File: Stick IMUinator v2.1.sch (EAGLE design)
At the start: 58 parts, among them J001 USB_MICROB_JST, J301 JST 2mm, J401 M06, J701 MICROSD-SOCKET, Q050 PMOS, Q201 PMOS, U101 BMP085, U201 5319, U301 73831, U401 LPC2148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

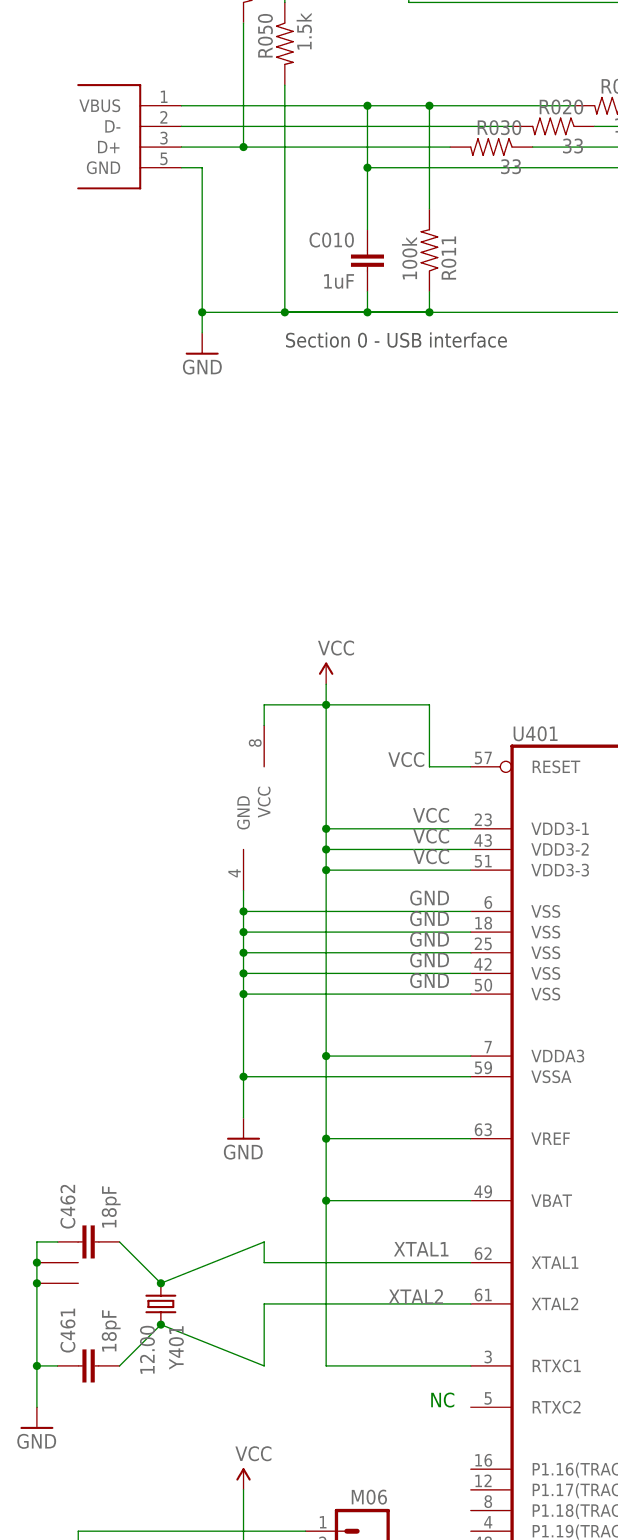
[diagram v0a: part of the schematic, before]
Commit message: Merged Mio's KwanSystems.lbr, updated all eagle files to use it.
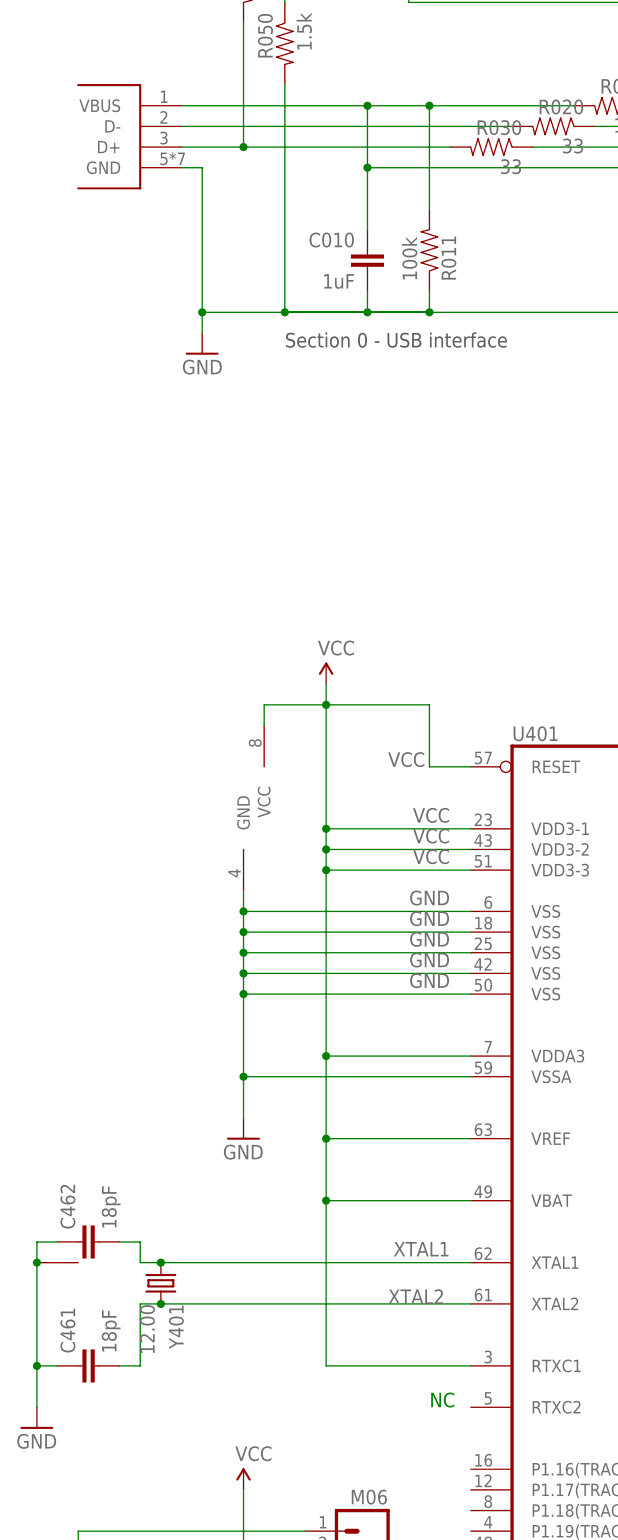
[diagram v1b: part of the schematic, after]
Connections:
- net GND: no longer Y401G$2.1
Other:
- moved on the sheet: Y401
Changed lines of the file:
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@@
 <?xml version="1.0" encoding="utf-8"?>
 <!DOCTYPE eagle SYSTEM "eagle.dtd">
-<eagle version="6.1">
+<eagle version="6.2">
 <drawing>
 <settings>
@@
 <attribute name="DIGIKEY" x="22.86" y="-101.6" size="1.778" layer="96" rot="MR180" display="off"/>
 </instance>
-<instance part="Y401" gate="G$2" x="22.86" y="-104.14" rot="R270"/>
-<instance part="Y401" gate="_" x="38.1" y="-106.68" rot="R270"/>
+<instance part="Y401" gate="_" x="38.1" y="-104.14" rot="R270"/>
 <instance part="R401" gate="A" x="165.1" y="-38.1" rot="R90">
 <attribute name="DIGIKEY" x="165.1" y="-38.1" size="1.778" layer="96" rot="MR180" display="off"/>
@@
 <wire x1="25.4" y1="-99.06" x2="22.86" y2="-99.06" width="0.1524" layer="91"/>
 <wire x1="22.86" y1="-99.06" x2="22.86" y2="-101.6" width="0.1524" layer="91"/>
-<wire x1="22.86" y1="-101.6" x2="22.86" y2="-104.14" width="0.1524" layer="91"/>
-<wire x1="22.86" y1="-104.14" x2="22.86" y2="-114.3" width="0.1524" layer="91"/>
+<wire x1="22.86" y1="-101.6" x2="22.86" y2="-114.3" width="0.1524" layer="91"/>
 <wire x1="22.86" y1="-114.3" x2="22.86" y2="-119.38" width="0.1524" layer="91"/>
 <wire x1="25.4" y1="-114.3" x2="22.86" y2="-114.3" width="0.1524" layer="91"/>
 <junction x="22.86" y="-114.3"/>
 <junction x="22.86" y="-101.6"/>
-<junction x="22.86" y="-104.14"/>
 <pinref part="C462" gate="G$1" pin="1"/>
 <pinref part="C461" gate="G$1" pin="1"/>
 <pinref part="GND2" gate="1" pin="GND"/>
 <pinref part="Y401" gate="G$1" pin="1"/>
-<pinref part="Y401" gate="G$2" pin="1"/>
 </segment>
 <segment>
@@
 <net name="XTAL1" class="0">
 <segment>
-<wire x1="33.02" y1="-99.06" x2="38.1" y2="-104.14" width="0.1524" layer="91"/>
-<wire x1="38.1" y1="-104.14" x2="50.8" y2="-99.06" width="0.1524" layer="91"/>
-<wire x1="50.8" y1="-99.06" x2="50.8" y2="-101.6" width="0.1524" layer="91"/>
-<wire x1="50.8" y1="-101.6" x2="76.2" y2="-101.6" width="0.1524" layer="91"/>
-<junction x="38.1" y="-104.14"/>
+<wire x1="33.02" y1="-99.06" x2="35.56" y2="-99.06" width="0.1524" layer="91"/>
+<wire x1="35.56" y1="-99.06" x2="35.56" y2="-101.6" width="0.1524" layer="91"/>
+<wire x1="35.56" y1="-101.6" x2="38.1" y2="-101.6" width="0.1524" layer="91"/>
+<wire x1="38.1" y1="-101.6" x2="76.2" y2="-101.6" width="0.1524" layer="91"/>
+<junction x="38.1" y="-101.6"/>
 <label x="73.66" y="-99.06" size="1.778" layer="95" rot="R180"/>
 <pinref part="C462" gate="G$1" pin="2"/>
@@
 <net name="XTAL2" class="0">
 <segment>
-<wire x1="50.8" y1="-114.3" x2="38.1" y2="-109.22" width="0.1524" layer="91"/>
-<wire x1="38.1" y1="-109.22" x2="33.02" y2="-114.3" width="0.1524" layer="91"/>
-<wire x1="50.8" y1="-114.3" x2="50.8" y2="-106.68" width="0.1524" layer="91"/>
-<wire x1="50.8" y1="-106.68" x2="76.2" y2="-106.68" width="0.1524" layer="91"/>
-<junction x="38.1" y="-109.22"/>
+<wire x1="38.1" y1="-106.68" x2="35.56" y2="-106.68" width="0.1524" layer="91"/>
+<wire x1="35.56" y1="-106.68" x2="35.56" y2="-114.3" width="0.1524" layer="91"/>
+<wire x1="35.56" y1="-114.3" x2="33.02" y2="-114.3" width="0.1524" layer="91"/>
+<wire x1="38.1" y1="-106.68" x2="76.2" y2="-106.68" width="0.1524" layer="91"/>
+<junction x="38.1" y="-106.68"/>
 <label x="66.04" y="-106.68" size="1.778" layer="95"/>
 <pinref part="C461" gate="G$1" pin="2"/>
